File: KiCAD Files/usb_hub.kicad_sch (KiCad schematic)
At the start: 27 parts, among them IC1 USB2512B-I_M2, IC2 LDK120C33R, IC3 LAN9500AI-ABZJ-TR, J3 J0011D01BNL, Y1 ABM8G-24.000MHZ-18-D2Y-T

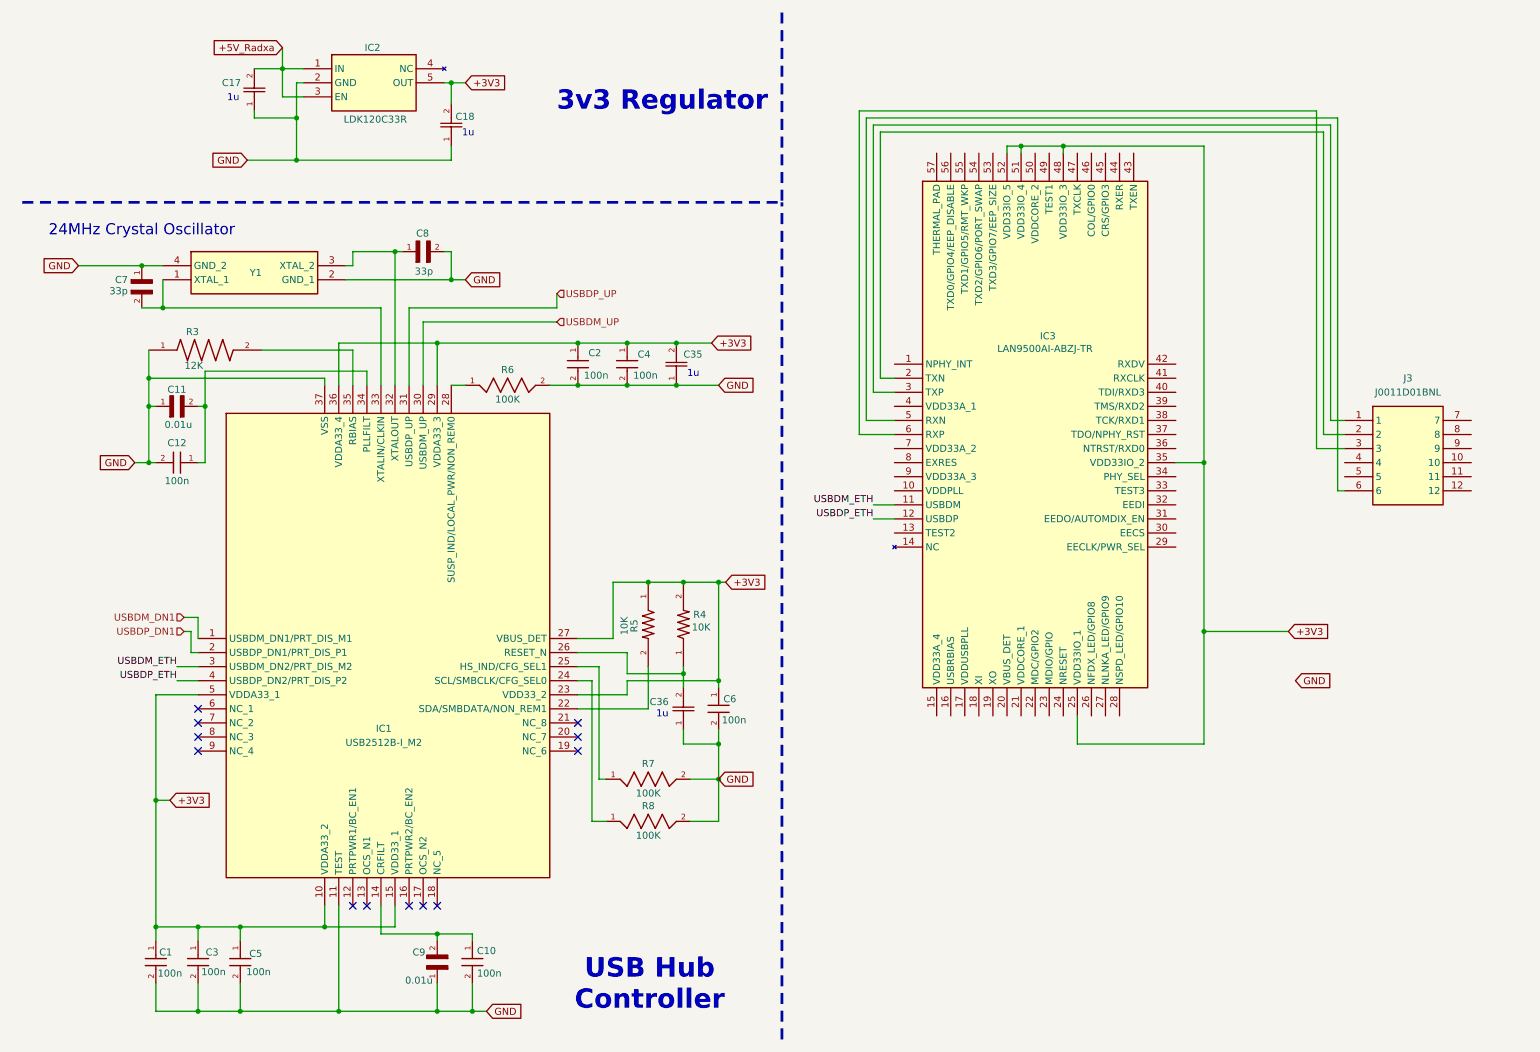
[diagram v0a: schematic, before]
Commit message: Ethernet routing pending
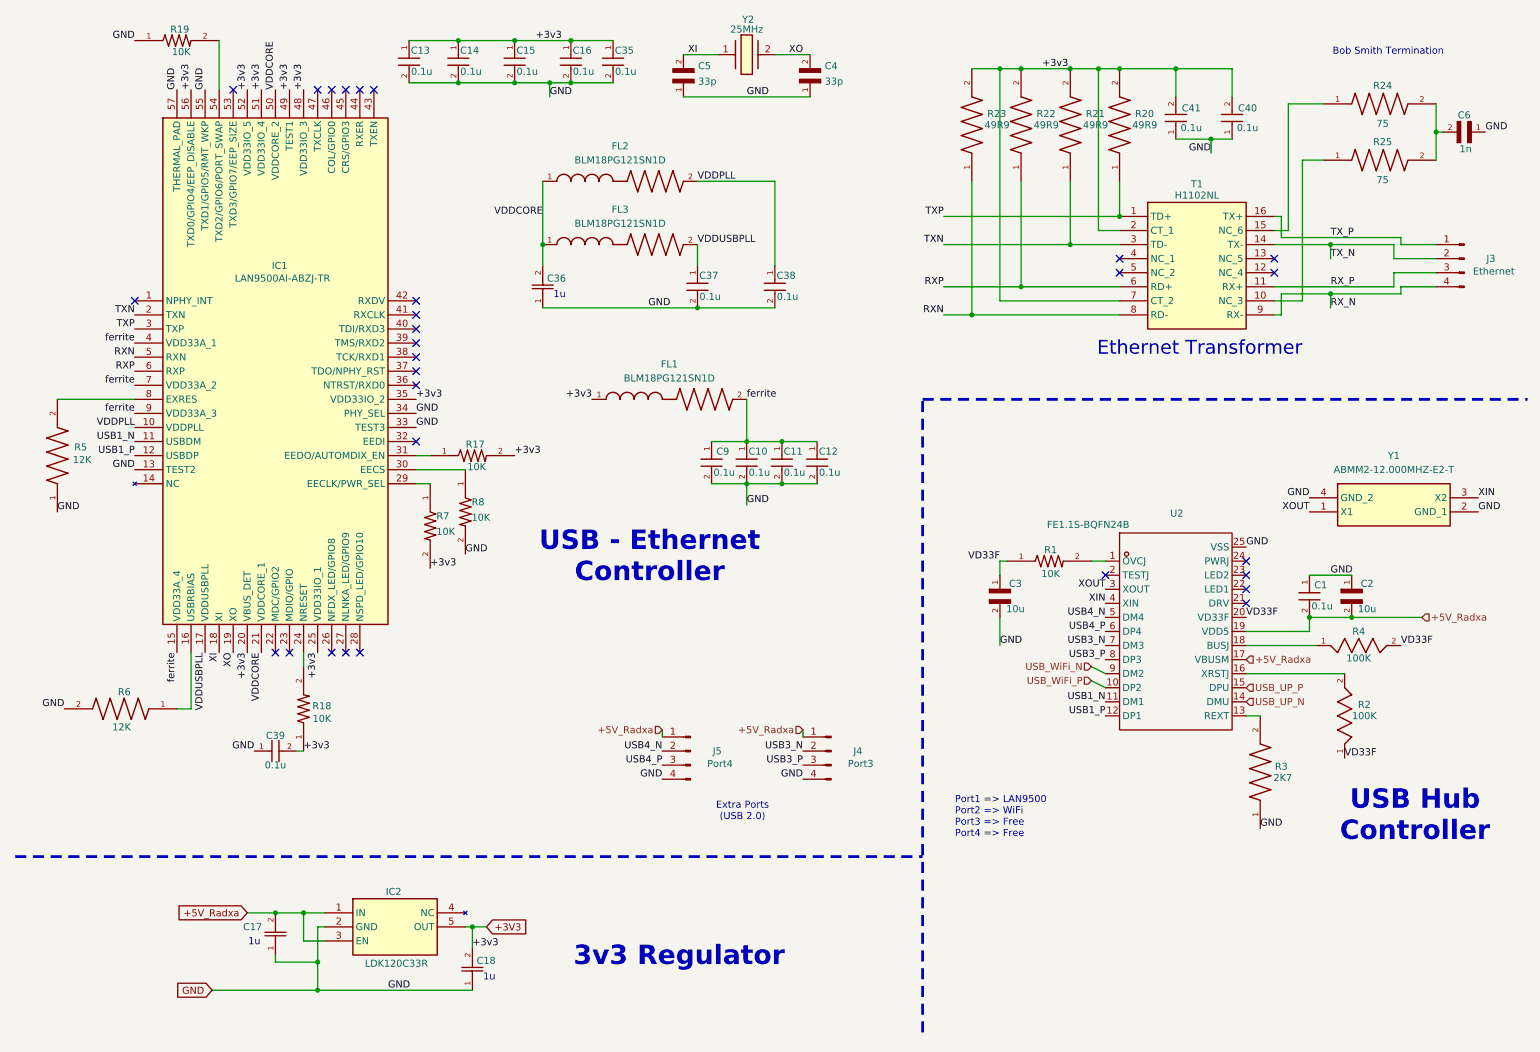
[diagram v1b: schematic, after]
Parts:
- removed C11, C9: 0.01u, GCD188R71H103KA01D:CAPC1608X90N, symbol GCD188R71H103KA01D:GCD188R71H103KA01D
- removed C2, C3, C4, C5, C6: 100n, Package_SO:SOIC-8_3.9x4.9mm_P1.27mm, symbol 100nF0603:WCAP-CSGP_0603
- removed C35: 1uF, CC0805KKX7R6BB225:CAPC2013X145N, symbol CC0805KKX7R6BB225:CC0805KKX7R6BB225
- removed C7, C8: 33p, TCC0402COG330J500AT:CAPC1005X55N, symbol TCC0402COG330J500AT:TCC0402COG330J500AT
- removed IC1: USB2512B-I_M2, QFN50P600X600X100-37N-D, symbol USB2512B-I_M2:USB2512B-I_M2
- removed IC3: LAN9500AI-ABZJ-TR, QFN50P800X800X100-57N-D, symbol LAN9500AI-ABZJ-TR:LAN9500AI-ABZJ-TR
- removed J3: J0011D01BNL, J0011D21BNL, symbol J0011D01BNL:J0011D01BNL
- removed R3: 12K, RC0805FR-0712KL:RESC2012X60N, symbol RC0805FR-0712KL:RC0805FR-0712KL
- removed R4, R5: 10K, RC0603JR-0710KL:RESC1607X60N, symbol RC0603JR-0710KL:RC0603JR-0710KL
- removed R6, R7, R8: 100K, RC0402FR-07100KL:RESC1005X40, symbol RC0402FR-07100KL:RC0402FR-07100KL
- removed Y1: ABM8G-24.000MHZ-18-D2Y-T, ABM8G, symbol ABM8G-24_000MHZ-18-D2Y-T:ABM8G-24.000MHZ-18-D2Y-T
- added C11, C13, C14, C15, C16, C35, C37, C38, C39, C40, C41, C9: 0.1u, Footprints:100nF0603, symbol 100nF0603:WCAP-CSGP_0603
- added C2, C3: 10u, Footprints:CL10A106KQ8NNNC, symbol CL10A106KQ8NNNC:CL10A106KQ8NNNC
- added C4, C5: 33p, Footprints:TCC0402COG330J500AT, symbol TCC0402COG330J500AT:TCC0402COG330J500AT
- added C6: 1n, Footprints:C1206C102JGRACTU, symbol C1206C102JGRACTU:C1206C102JGRACTU
- added FL1, FL2, FL3: BLM18PG121SN1D, Footprints:BLM18PG121SN1D, symbol BLM18PG121SN1D:BLM18PG121SN1D
- added IC1: LAN9500AI-ABZJ-TR, Footprints:LAN9500AI-ABZJ-TR, symbol LAN9500AI-ABZJ-TR:LAN9500AI-ABZJ-TR
- added J3: Ethernet, Connector_JST:JST_GH_SM04B-GHS-TB_1x04-1MP_P1.25mm_Horizontal, symbol Connector:Conn_01x04_Pin
- added J4: Port3, Connector_JST:JST_GH_SM04B-GHS-TB_1x04-1MP_P1.25mm_Horizontal, symbol Connector:Conn_01x04_Pin
- added J5: Port4, Connector_JST:JST_GH_SM04B-GHS-TB_1x04-1MP_P1.25mm_Horizontal, symbol Connector:Conn_01x04_Pin
- added R1, R17, R18, R19, R7, R8: 10K, Footprints:RC0603JR-0710KL, symbol RC0603JR-0710KL:RC0603JR-0710KL
- added R2, R4: 100K, Footprints:RC0402FR-07100KL, symbol RC0402FR-07100KL:RC0402FR-07100KL
- added R20, R21, R22, R23: 49R9, Footprints:RC0805FR-0749R9L, symbol RC0805FR-0749R9L:RC0805FR-0749R9L
- added R24, R25: 75, Footprints:RC0805FR-0775RL, symbol RC0805FR-0775RL:RC0805FR-0775RL
- added R3: 2K7, Footprints:RC0805FR-072K7L, symbol RC0805FR-072K7L:RC0805FR-072K7L
- added R5, R6: 12K, Footprints:RC0805FR-0712KL, symbol RC0805FR-0712KL:RC0805FR-0712KL
- added T1: H1102NL, Footprints:H1102NL, symbol H1102NL:H1102NL
- added U2: FE1.1S-BQFN24B, Footprints:FE1.1S-BQFN24B, symbol P1-altium-import:root_0_FE1.1S-BQFN24B_
- added Y1: ABMM2-12.000MHZ-E2-T, Footprints:ABMM2-12MHz, symbol ABMM2-12_000MHZ-E2-T:ABMM2-12.000MHZ-E2-T
- added Y2: 25MHz, Footprints:ABM7-25MHz, symbol ABM7-25_000MHZ-D2Y-T:ABM7-25.000MHZ-D2Y-T
- C1, C10, C12: value 100n -> 0.1u; footprint Package_SO:SOIC-8_3.9x4.9mm_P1.27mm -> Footprints:100nF0603
- C17, C18: footprint CC0805KKX7R6BB225:CAPC2013X145N -> Footprints:CC0805KKX7R6BB225
- C36: footprint CC0805KKX7R6BB225:CAPC2013X145N -> Footprints:C0805X474K101T
- IC2: footprint SOT65P210X110-5N -> Footprints:LDK120C33R
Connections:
- net +3V3: now also C13.1, C14.1, C15.1, C16.1, C35.1, C39.2, C40.2, C41.2, FL1.1, IC1.20 (VBUS_DET), IC1.25 (VDD33IO_1), IC1.35 (VDD33IO_2), IC1.48 (VDD33IO_3), IC1.49 (TEST1), IC1.51 (VDD33IO_4), IC1.52 (VDD33IO_5), IC1.56 (TXD0/GPIO4/EEP_DISABLE), R17.2, R18.1, R20.2, R21.2, R22.2, R23.2, R7.2, T1.2 (CT_1), T1.7 (CT_2); no longer C1.1
- net +5V_Radxa: now also C1.2, C2.2, J4.1 (Pin_1), J5.1 (Pin_1), U2.17 (VBUSM), U2.19 (VDD5)
- net GND: now also C1.1, C11.2, C13.2, C14.2, C15.2, C16.2, C2.1, C3.2, C35.2, C37.2, C38.2, C39.1, C4.1, C40.1, C41.1, C5.1, C6.1, C9.2, IC1.13 (TEST2), IC1.33 (TEST3), IC1.34 (PHY_SEL), IC1.55 (TXD1/GPIO5/RMT_WKP), IC1.57 (THERMAL_PAD), J4.4 (Pin_4), J5.4 (Pin_4), R19.1, R3.1, R5.1, R6.2, R8.2, U2.25 (VSS), Y1.2 (GND_1), Y1.4 (GND_2); no longer C1.2
- net ferrite: now reaches C12.1
- net ferrite: now also C10.1, C11.1, C9.1, FL1.2, IC1.15 (VDD33A_4), IC1.4 (VDD33A_1), IC1.7 (VDD33A_2), IC1.9 (VDD33A_3)
- net VDDCORE: now reaches C36.2
- net VDDCORE: now also FL2.1, FL3.1, IC1.21 (VDDCORE_1), IC1.50 (VDDCORE_2)
- new net: R25.1, T1.10 (NC_3)
- new net: R24.1, T1.15 (NC_6)
- new net: IC1.16 (USBRBIAS), R6.1
- new net: R2.2, U2.16 (XRSTJ)
- new net: C6.2, R24.2, R25.2
- new net: IC1.8 (EXRES), R5.2
- new net: R1.2, U2.1 (OVCJ)
- new net: R3.2, U2.13 (REXT)
- new net: R4.1, U2.18 (BUSJ)
- new net: IC1.54 (TXD2/GPIO6/PORT_SWAP), R19.2
- new net: IC1.24 (NRESET), R18.2
- new net: IC1.29 (EECLK/PWR_SEL), R7.1
- new net: IC1.30 (EECS), R8.1
- new net: IC1.31 (EEDO/AUTOMDIX_EN), R17.1
- new net RXN: IC1.5 (RXN), R23.1, T1.8 (RD-)
- new net RXP: IC1.6 (RXP), R22.1, T1.6 (RD+)
- new net RX_N: J3.4 (Pin_4), T1.9 (RX-)
- new net RX_P: J3.3 (Pin_3), T1.11 (RX+)
- new net TXN: IC1.2 (TXN), R21.1, T1.3 (TD-)
- new net TXP: IC1.3 (TXP), R20.1, T1.1 (TD+)
- new net TX_N: J3.2 (Pin_2), T1.14 (TX-)
- new net TX_P: J3.1 (Pin_1), T1.16 (TX+)
- new net USB1_N: IC1.11 (USBDM), U2.11 (DM1)
- new net USB1_P: IC1.12 (USBDP), U2.12 (DP1)
- new net USB3_N: J4.2 (Pin_2), U2.7 (DM3)
- new net USB3_P: J4.3 (Pin_3), U2.8 (DP3)
- new net USB4_N: J5.2 (Pin_2), U2.5 (DM4)
- new net USB4_P: J5.3 (Pin_3), U2.6 (DP4)
- new net USB_UP_N: U2.14 (DMU)
- new net USB_UP_P: U2.15 (DPU)
- new net USB_WiFi_N: U2.9 (DM2)
- new net USB_WiFi_P: U2.10 (DP2)
- new net VD33F: C3.1, R1.1, R2.1, R4.2, U2.20 (VD33F)
- new net VDDPLL: C38.1, FL2.2, IC1.10 (VDDPLL)
- new net VDDUSBPLL: C37.1, FL3.2, IC1.17 (VDDUSBPLL)
- new net XI: C5.2, IC1.18 (XI), Y2.1
- new net XIN: U2.4 (XIN), Y1.3 (X2)
- new net XO: C4.2, IC1.19 (XO), Y2.2
- new net XOUT: U2.3 (XOUT), Y1.1 (X1)
- no-connect marks 12 -> 29
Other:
- note added: "Bob Smith Termination"
- note added: "Ethernet Transformer"
- note added: "Extra Ports (USB 2.0)"
- note added: "Port1 => LAN9500 Port2 => WiFi Port3 => Free Port4 => Free"
- note added: "USB - Ethernet Controller"
- note removed: "24MHz Crystal Oscillator"
- moved on the sheet: C17, C18, IC2
